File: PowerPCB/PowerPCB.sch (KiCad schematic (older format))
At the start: 22 parts, among them J1 Conn_01x03_Male, J2 Conn_01x10_Male, J3 STM Inputs, J4 STM Outputs, J5 Conn_01x07_Male, K1 1721081-5, K2 1721081-5, U1 NCP1117-3.3_SOT223, U2 STM32F413ZHTx

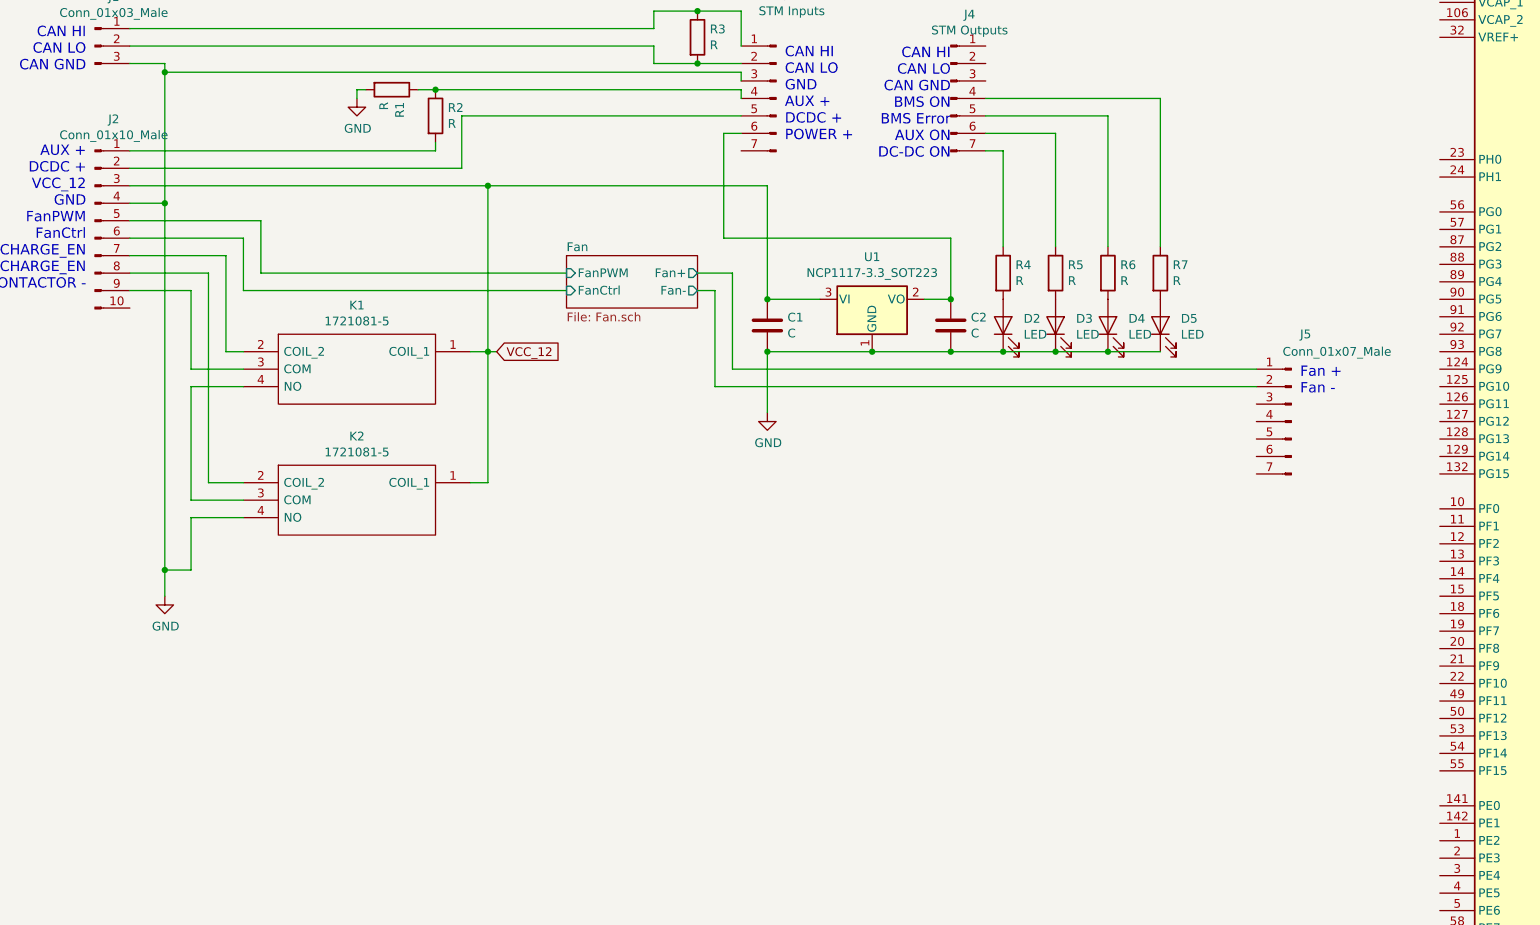
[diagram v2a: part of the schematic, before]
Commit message: Cleaned up main schematic and corrected text for fan relay
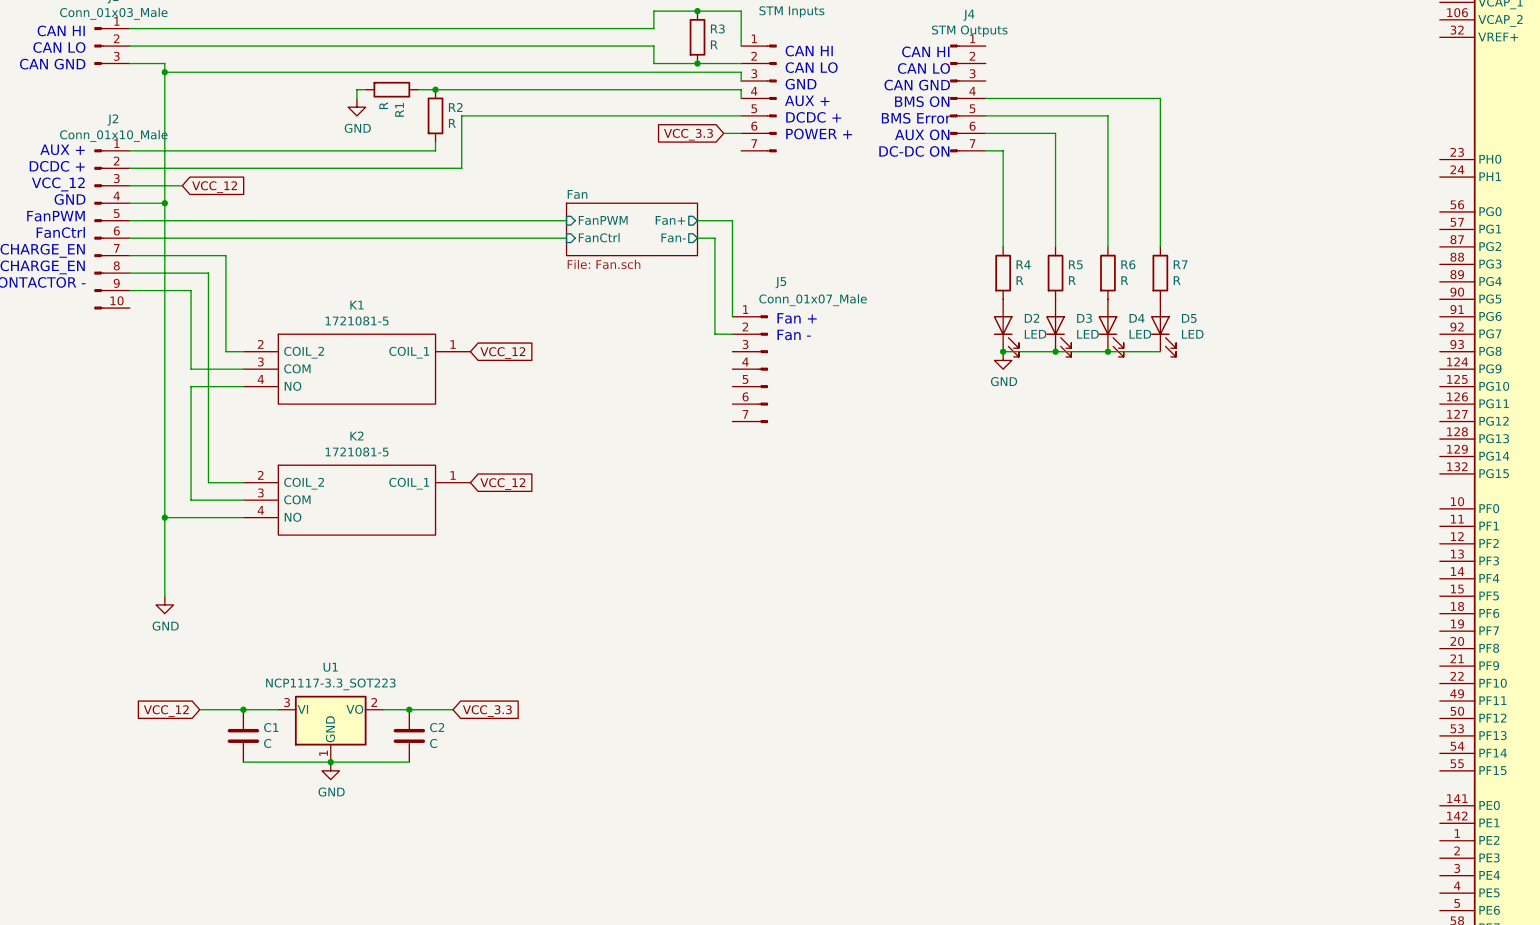
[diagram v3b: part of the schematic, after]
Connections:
- net VCC_3.3: now reaches C2.1, J3.6 (Pin_6), U1.2 (VO)
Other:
- moved on the sheet: C1, C2, J5, U1
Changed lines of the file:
@@
 Wire Wire Line
 	1500 1650 1700 1650
-Wire Wire Line
-	5150 3300 5750 3300
 $Comp
 L Device:C C1
 U 1 1 5E9AFBC4
-P 5150 3150
-F 0 "C1" H 5265 3196 50  0000 L CNN
-F 1 "C" H 5265 3105 50  0000 L CNN
-F 2 "Capacitor_SMD:C_0805_2012Metric_Pad1.15x1.40mm_HandSolder" H 5188 3000 50  0001 C CNN
-F 3 "~" H 5150 3150 50  0001 C CNN
-	1    5150 3150
-	1    0    0    -1
-$EndComp
-Wire Wire Line
-	5750 3300 6200 3300
-Connection ~ 6200 3000
+P 2150 5500
+F 0 "C1" H 2265 5546 50  0000 L CNN
+F 1 "C" H 2265 5455 50  0000 L CNN
+F 2 "Capacitor_SMD:C_0805_2012Metric_Pad1.15x1.40mm_HandSolder" H 2188 5350 50  0001 C CNN
+F 3 "~" H 2150 5500 50  0001 C CNN
+	1    2150 5500
+	1    0    0    -1
+$EndComp
+Wire Wire Line
+	2650 5650 3100 5650
 $Comp
 L Device:C C2
 U 1 1 5E9AEA5E
-P 6200 3150
-F 0 "C2" H 6315 3196 50  0000 L CNN
-F 1 "C" H 6315 3105 50  0000 L CNN
-F 2 "Capacitor_SMD:C_0805_2012Metric_Pad1.15x1.40mm_HandSolder" H 6238 3000 50  0001 C CNN
-F 3 "~" H 6200 3150 50  0001 C CNN
-	1    6200 3150
-	1    0    0    -1
-$EndComp
-Wire Wire Line
-	6050 3000 6200 3000
-Wire Wire Line
-	6200 2650 6200 3000
-Wire Wire Line
-	4900 2650 6200 2650
-Wire Wire Line
-	4900 2050 4900 2650
-Wire Wire Line
-	5450 3000 5150 3000
-Connection ~ 5750 3300
+P 3100 5500
+F 0 "C2" H 3215 5546 50  0000 L CNN
+F 1 "C" H 3215 5455 50  0000 L CNN
+F 2 "Capacitor_SMD:C_0805_2012Metric_Pad1.15x1.40mm_HandSolder" H 3138 5350 50  0001 C CNN
+F 3 "~" H 3100 5500 50  0001 C CNN
+	1    3100 5500
+	1    0    0    -1
+$EndComp
+Wire Wire Line
+	2950 5350 3100 5350
+Wire Wire Line
+	2350 5350 2150 5350
+Connection ~ 2650 5650
 $Comp
 L Regulator_Linear:NCP1117-3.3_SOT223 U1
 U 1 1 5E9953A6
-P 5750 3000
-F 0 "U1" H 5750 3242 50  0000 C CNN
-F 1 "NCP1117-3.3_SOT223" H 5750 3151 50  0000 C CNN
-F 2 "Package_TO_SOT_SMD:SOT-223-3_TabPin2" H 5750 3200 50  0001 C CNN
-F 3 "http://www.onsemi.com/pub_link/Collateral/NCP1117-D.PDF" H 5850 2750 50  0001 C CNN
-	1    5750 3000
+P 2650 5350
+F 0 "U1" H 2650 5592 50  0000 C CNN
+F 1 "NCP1117-3.3_SOT223" H 2650 5501 50  0000 C CNN
+F 2 "Package_TO_SOT_SMD:SOT-223-3_TabPin2" H 2650 5550 50  0001 C CNN
+F 3 "http://www.onsemi.com/pub_link/Collateral/NCP1117-D.PDF" H 2750 5100 50  0001 C CNN
+	1    2650 5350
 	1    0    0    -1
 $EndComp
@@
 L Connector:Conn_01x07_Male J5
 U 1 1 5E941799
-P 8150 3700
-F 0 "J5" H 8100 4200 50  0000 R CNN
-F 1 "Conn_01x07_Male" H 8200 4100 50  0000 R CNN
-F 2 "Connector_PinHeader_2.54mm:PinHeader_1x07_P2.54mm_Horizontal" H 8150 3700 50  0001 C CNN
-F 3 "~" H 8150 3700 50  0001 C CNN
-	1    8150 3700
+P 5150 3400
+F 0 "J5" H 5100 3900 50  0000 R CNN
+F 1 "Conn_01x07_Male" H 5200 3800 50  0000 R CNN
+F 2 "Connector_PinHeader_2.54mm:PinHeader_1x07_P2.54mm_Horizontal" H 5150 3400 50  0001 C CNN
+F 3 "~" H 5150 3400 50  0001 C CNN
+	1    5150 3400
 	-1   0    0    -1
 $EndComp
@@
 CAN HI\nCAN LO\nCAN GND\nBMS ON\nBMS Error\nAUX ON\nDC-DC ON
 Wire Wire Line
-	6200 3300 6500 3300
-Connection ~ 6200 3300
-Wire Wire Line
 	6400 2050 6800 2050
 Wire Wire Line
@@
 	0    -1   -1   0
 $EndComp
-Connection ~ 6500 3300
 Wire Wire Line
 	6500 3300 6800 3300
@@
 	6500 2150 6400 2150
 $Sheet
-S 4000 2750 750  300
+S 4000 2450 750  300
 U 5EC1CC82
 F0 "Fan" 50
 F1 "Fan.sch" 50
-F2 "FanPWM" I L 4000 2850 50
-F3 "Fan+" O R 4750 2850 50
-F4 "Fan-" O R 4750 2950 50
-F5 "FanCtrl" I L 4000 2950 50
+F2 "FanPWM" I L 4000 2550 50
+F3 "Fan+" O R 4750 2550 50
+F4 "Fan-" O R 4750 2650 50
+F5 "FanCtrl" I L 4000 2650 50
 $EndSheet
 $Comp
@@
 $EndComp
 Wire Wire Line
-	4950 3400 4950 2850
-Wire Wire Line
-	4950 2850 4750 2850
-Wire Wire Line
-	4950 3400 7950 3400
-Wire Wire Line
-	4850 3500 4850 2950
-Wire Wire Line
-	4850 2950 4750 2950
-Wire Wire Line
-	4850 3500 7950 3500
-Wire Wire Line
-	1500 2550 2250 2550
-Wire Wire Line
-	2250 2850 4000 2850
-Wire Wire Line
-	1500 2650 2150 2650
-Wire Wire Line
-	2150 2950 4000 2950
-Wire Wire Line
-	1700 4550 1850 4550
-Wire Wire Line
-	1700 4550 1700 4700
+	4950 3100 4950 2550
+Wire Wire Line
+	4950 2550 4750 2550
+Wire Wire Line
+	4850 3200 4850 2650
+Wire Wire Line
+	4850 2650 4750 2650
 $Comp
 L power:GND #PWR0101
@@
 	1    0    0    -1
 $EndComp
-Connection ~ 1700 4550
 Wire Wire Line
 	1500 2750 2050 2750
-Wire Wire Line
-	5150 3300 5150 3650
-Connection ~ 5150 3300
-Wire Wire Line
-	1700 2450 1700 4550
 Connection ~ 1700 2450
 Wire Wire Line
 	1500 2850 1950 2850
-Text GLabel 3600 3300 2    50   Input ~ 0
+Text GLabel 3450 3300 2    50   Input ~ 0
 VCC_12
 Wire Wire Line
-	3600 3300 3550 3300
-Wire Wire Line
-	3450 4050 3550 4050
-Wire Wire Line
-	3550 4050 3550 3300
-Connection ~ 3550 3300
-Wire Wire Line
-	3550 3300 3450 3300
-Wire Wire Line
 	2050 3300 2150 3300
 Wire Wire Line
@@
 	1850 4150 2150 4150
 Wire Wire Line
-	2150 4250 1850 4250
-Wire Wire Line
-	1850 4250 1850 4550
-Wire Wire Line
 	1700 1700 1700 2450
 Wire Wire Line
@@
 Wire Wire Line
 	2050 2750 2050 3300
-Wire Wire Line
-	2150 2650 2150 2950
-Wire Wire Line
-	2250 2550 2250 2850
-Wire Wire Line
-	3550 3300 3550 2350
-Wire Wire Line
-	1500 2350 3550 2350
-Wire Wire Line
-	3550 2350 5150 2350
-Wire Wire Line
-	5150 2350 5150 3000
-Connection ~ 3550 2350
-Connection ~ 5150 3000
-Text Notes 8200 3550 0    59   ~ 0
+Text Notes 5200 3250 0    59   ~ 0
 Fan +\nFan -
 $Comp
@@
 L power:GND #PWR?
 U 1 1 5ED64848
-P 5150 3650
-F 0 "#PWR?" H 5150 3400 50  0001 C CNN
-F 1 "GND" H 5155 3477 50  0000 C CNN
-F 2 "" H 5150 3650 50  0001 C CNN
-F 3 "" H 5150 3650 50  0001 C CNN
-	1    5150 3650
-	1    0    0    -1
-$EndComp
+P 2650 5650
+F 0 "#PWR?" H 2650 5400 50  0001 C CNN
+F 1 "GND" H 2655 5477 50  0000 C CNN
+F 2 "" H 2650 5650 50  0001 C CNN
+F 3 "" H 2650 5650 50  0001 C CNN
+	1    2650 5650
+	1    0    0    -1
+$EndComp
+Wire Wire Line
+	1700 2450 1700 4250
+Wire Wire Line
+	1700 4250 2150 4250
+Connection ~ 1700 4250
+Wire Wire Line
+	1700 4250 1700 4700
+Text GLabel 3450 4050 2    50   Input ~ 0
+VCC_12
+Wire Wire Line
+	2150 5650 2650 5650
+$Comp
+L power:GND #PWR?
+U 1 1 5ED77241
+P 6500 3300
+F 0 "#PWR?" H 6500 3050 50  0001 C CNN
+F 1 "GND" H 6505 3127 50  0000 C CNN
+F 2 "" H 6500 3300 50  0001 C CNN
+F 3 "" H 6500 3300 50  0001 C CNN
+	1    6500 3300
+	1    0    0    -1
+$EndComp
+Connection ~ 6500 3300
+Text GLabel 1900 5350 0    50   Input ~ 0
+VCC_12
+Connection ~ 2150 5350
+Text GLabel 3350 5350 2    50   Input ~ 0
+VCC_3.3
+Wire Wire Line
+	3350 5350 3100 5350
+Connection ~ 3100 5350
+Wire Wire Line
+	1900 5350 2150 5350
+Text GLabel 4900 2050 0    50   Input ~ 0
+VCC_3.3
+Text GLabel 1800 2350 2    50   Input ~ 0
+VCC_12
+Wire Wire Line
+	1500 2350 1800 2350
+Wire Wire Line
+	4950 3200 4850 3200
+Wire Wire Line
+	1500 2550 4000 2550
+Wire Wire Line
+	1500 2650 4000 2650
 $EndSCHEMATC

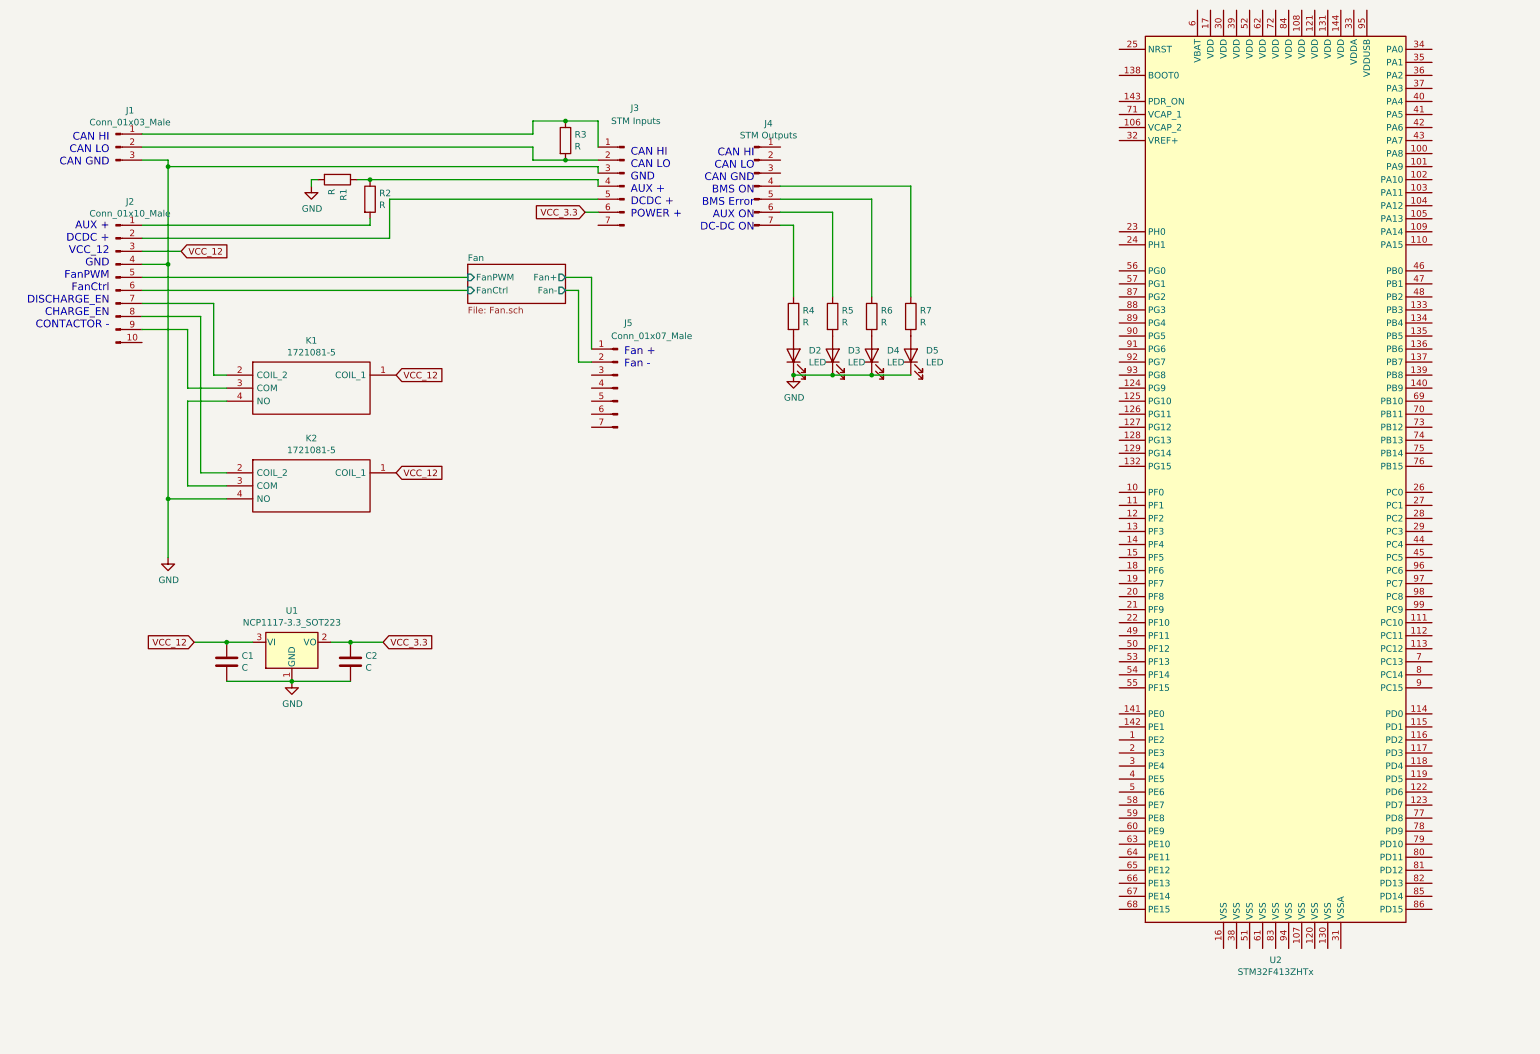
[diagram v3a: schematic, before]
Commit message: Added CAN connections to STM
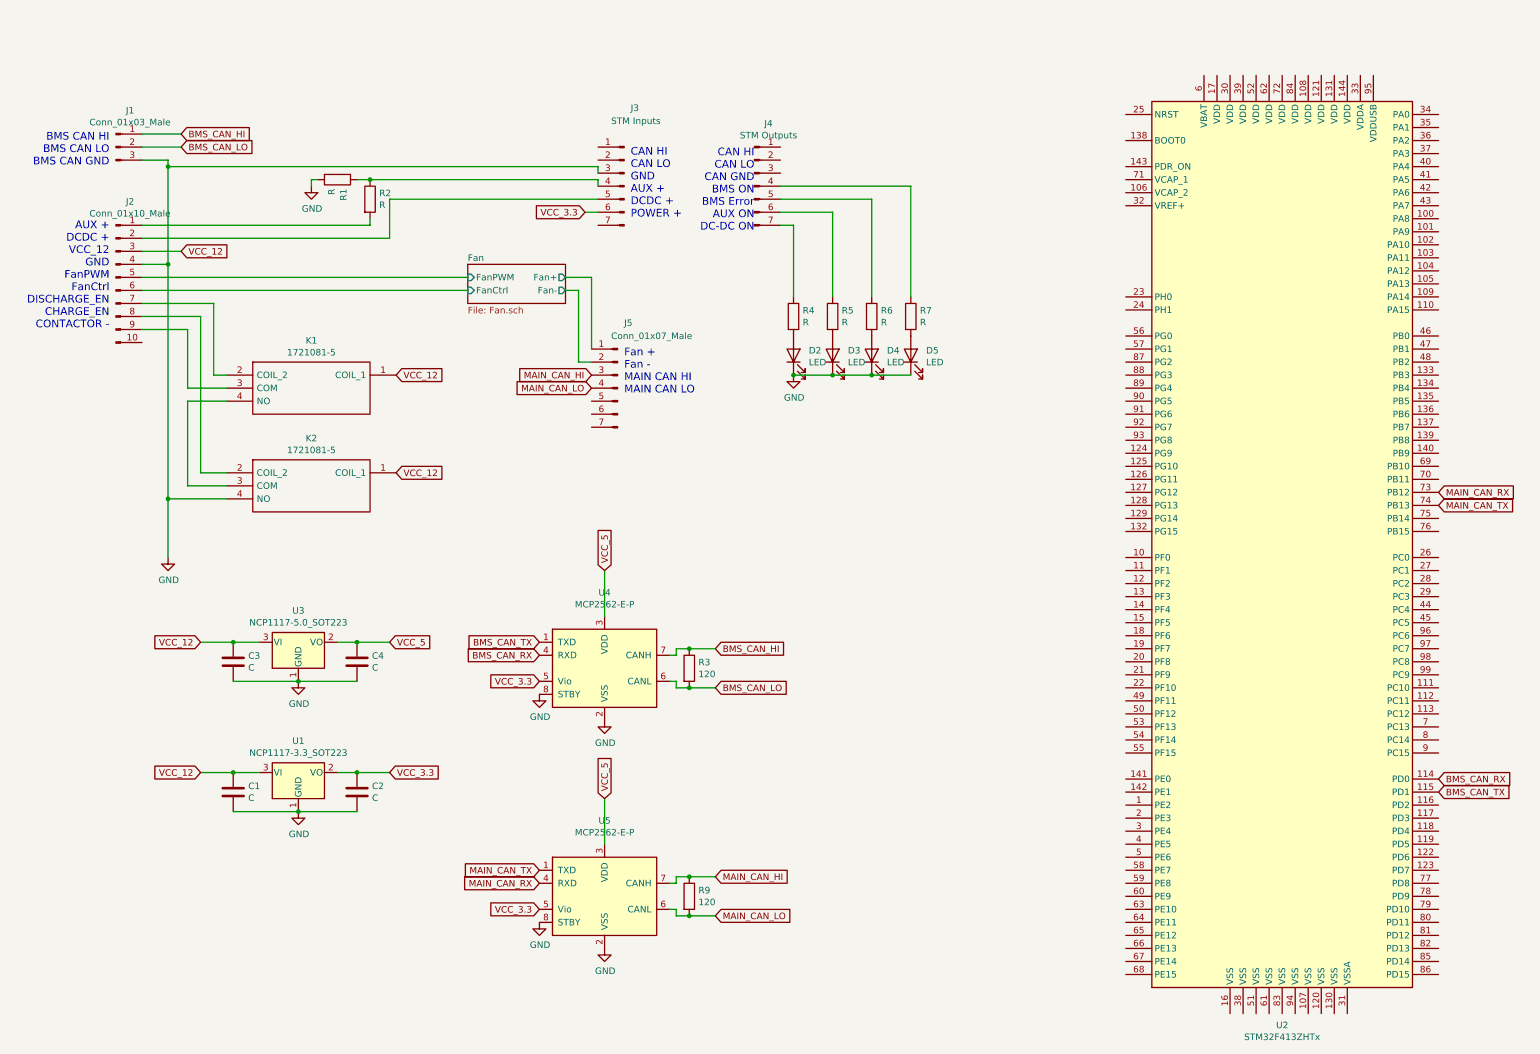
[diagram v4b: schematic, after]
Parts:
- added C3, C4: C, Capacitor_SMD:C_0805_2012Metric_Pad1.15x1.40mm_HandSolder, symbol Device:C
- added R9: 120, Resistor_SMD:R_0805_2012Metric_Pad1.15x1.40mm_HandSolder, symbol Device:R
- added U3: NCP1117-5.0_SOT223, Package_TO_SOT_SMD:SOT-223-3_TabPin2, symbol Regulator_Linear:NCP1117-5.0_SOT223
- added U4, U5: MCP2562-E-P, Package_DIP:DIP-8_W7.62mm, symbol Interface_CAN_LIN:MCP2562-E-P
- R3: value R -> 120
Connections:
- net GND: now also C3.2, C4.2, U3.1 (GND), U4.2 (VSS), U4.8 (STBY), U5.2 (VSS), U5.8 (STBY)
- net VCC_12: now also C3.1, U3.3 (VI)
- net VCC_3.3: now also U4.5 (Vio), U5.5 (Vio)
- net BMS_CAN_HI: now reaches J1.1 (Pin_1), R3.1
- net BMS_CAN_HI: now also U4.7 (CANH); no longer J3.1 (Pin_1)
- net BMS_CAN_LO: now reaches J1.2 (Pin_2), R3.2
- net BMS_CAN_LO: now also U4.6 (CANL); no longer J3.2 (Pin_2)
- net MAIN_CAN_HI: now reaches J5.3 (Pin_3)
- net MAIN_CAN_HI: now also R9.1, U5.7 (CANH)
- net MAIN_CAN_LO: now reaches J5.4 (Pin_4)
- net MAIN_CAN_LO: now also R9.2, U5.6 (CANL)
- net BMS_CAN_RX: now reaches U2.114 (PD0)
- net BMS_CAN_RX: now also U4.4 (RXD)
- net BMS_CAN_TX: now reaches U2.115 (PD1)
- net BMS_CAN_TX: now also U4.1 (TXD)
- net MAIN_CAN_RX: now reaches U2.73 (PB12)
- net MAIN_CAN_RX: now also U5.4 (RXD)
- net MAIN_CAN_TX: now reaches U2.74 (PB13)
- net MAIN_CAN_TX: now also U5.1 (TXD)
- new net VCC_5: C4.1, U3.2 (VO), U4.3 (VDD), U5.3 (VDD)
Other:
- note added: "BMS CAN HI\nBMS CAN LO\nBMS CAN GND"
- note added: "Fan +\nFan -\nMAIN CAN HI\nMAIN CAN LO"
- note removed: "CAN HI\nCAN LO\nCAN GND"
- note removed: "Fan +\nFan -"
- moved on the sheet: C1, C2, R3, U1, U2
